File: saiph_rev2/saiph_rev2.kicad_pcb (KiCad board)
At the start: 2 copper layers, 347.7 x 126.6 mm, 211 parts, among them J1 USB_mini_micro_B, J2 Conn_01x04, M1 MISC, SW1 SW_PUSH, SW10 SW_PUSH, SW100 SW_PUSH, SW101 SW_PUSH, SW102 SW_PUSH, SW103 SW_PUSH, SW104 SW_PUSH, SW105 SW_PUSH, SW108 SKQGABE010, SW109 SW_PUSH, SW11 SW_PUSH, SW110 SW_PUSH, SW111 SW_PUSH, SW112 SKQGABE010, SW12 SW_PUSH, SW13 SW_PUSH, SW14 SW_PUSH, SW15 SW_PUSH, SW16 SW_PUSH, SW17 SW_PUSH, SW18 SW_PUSH, SW19 SW_PUSH, SW2 SW_PUSH, SW20 SW_PUSH, SW21 SW_PUSH, SW22 SW_PUSH, SW23 SW_PUSH, SW24 SW_PUSH, SW25 SW_PUSH, SW26 SW_PUSH, SW27 SW_PUSH, SW28 SW_PUSH, SW29 SW_PUSH, SW3 SW_PUSH, SW30 SW_PUSH, SW31 SW_PUSH, SW32 SW_PUSH, SW33 SW_PUSH, SW34 SW_PUSH, SW35 SW_PUSH, SW36 SW_PUSH, SW37 SW_PUSH, SW38 SW_PUSH, SW39 SW_PUSH, SW4 SW_PUSH, SW40 SW_PUSH, SW41 SW_PUSH, SW42 SW_PUSH, SW43 SW_PUSH, SW44 SW_PUSH, SW45 SW_PUSH, SW46 SW_PUSH, SW47 SW_PUSH, SW48 SW_PUSH, SW49 SW_PUSH, SW5 SW_PUSH, SW50 SW_PUSH, SW51 SW_PUSH, SW52 SW_PUSH, SW53 SW_PUSH, SW54 SW_PUSH, SW55 SW_PUSH, SW56 SW_PUSH, SW57 SW_PUSH, SW58 SW_PUSH, SW59 SW_PUSH, SW6 SW_PUSH, SW60 SW_PUSH, SW61 SW_PUSH, SW62 SW_PUSH, SW63 SW_PUSH, SW64 SW_PUSH, SW65 SW_PUSH, SW66 SW_PUSH, SW67 SW_PUSH, SW68 SW_PUSH, SW69 SW_PUSH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

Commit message: place r4 diodes
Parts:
- moved D72 7.37 mm to (245.2, 71.3), turned to 90 degrees
- moved D35 1.03 mm to (119.0, 71.3)
- moved D31 0.76 mm to (100.0, 63.7)
- moved D96 0.61 mm to (319.1, 63.7)
- moved D51 0.57 mm to (176.2, 63.7)
- moved D61 0.55 mm to (214.3, 63.7)
- moved D46 0.50 mm to (157.2, 71.3)
- moved D56 0.48 mm to (195.2, 71.3)
- moved D26 0.30 mm to (81.0, 71.3)
- moved D21 0.22 mm to (62.0, 63.7)
- moved D84 0.16 mm to (281.0, 63.7)
- moved D15 0.12 mm to (42.9, 71.3)
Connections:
- D72 pad 1: Net-(D72-K) -> /R3
- D72 pad 2: /R3 -> Net-(D72-A)
- SW72 pad 2: Net-(D72-K) -> Net-(D72-A)
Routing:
- net /R3: track 87.8 -> 93.1 mm
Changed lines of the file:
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@@
   (net 76 "Net-(D70-K)")
   (net 77 "Net-(D71-K)")
-  (net 78 "Net-(D72-K)")
+  (net 78 "Net-(D72-A)")
   (net 79 "Net-(D73-K)")
   (net 80 "Net-(D74-K)")
@@
   )
   (footprint "Diodes_ThroughHole:D_DO-35_SOD27_P7.62mm_Horizontal" (layer "F.Cu")
-    (at 42.75 71.325 90)
+    (at 42.875 71.325 90)
     (descr "D, DO-35_SOD27 series, Axial, Horizontal, pin pitch=7.62mm, , length*diameter=4*2mm^2, , http://www.diodes.com/_files/packages/DO-35.pdf")
     (tags "D DO-35_SOD27 series Axial Horizontal pin pitch 7.62mm  length 4mm diameter 2mm")
@@
   )
   (footprint "Diodes_ThroughHole:D_DO-35_SOD27_P7.62mm_Horizontal" (layer "F.Cu")
-    (at 62 63.925 -90)
+    (at 62 63.705 -90)
     (descr "D, DO-35_SOD27 series, Axial, Horizontal, pin pitch=7.62mm, , length*diameter=4*2mm^2, , http://www.diodes.com/_files/packages/DO-35.pdf")
     (tags "D DO-35_SOD27 series Axial Horizontal pin pitch 7.62mm  length 4mm diameter 2mm")
@@
   )
   (footprint "Diodes_ThroughHole:D_DO-35_SOD27_P7.62mm_Horizontal" (layer "F.Cu")
-    (at 81.14 71.575 90)
+    (at 80.975 71.325 90)
     (descr "D, DO-35_SOD27 series, Axial, Horizontal, pin pitch=7.62mm, , length*diameter=4*2mm^2, , http://www.diodes.com/_files/packages/DO-35.pdf")
     (tags "D DO-35_SOD27 series Axial Horizontal pin pitch 7.62mm  length 4mm diameter 2mm")
@@
   )
   (footprint "Diodes_ThroughHole:D_DO-35_SOD27_P7.62mm_Horizontal" (layer "F.Cu")
-    (at 99.49 64.27 -90)
+    (at 100 63.705 -90)
     (descr "D, DO-35_SOD27 series, Axial, Horizontal, pin pitch=7.62mm, , length*diameter=4*2mm^2, , http://www.diodes.com/_files/packages/DO-35.pdf")
     (tags "D DO-35_SOD27 series Axial Horizontal pin pitch 7.62mm  length 4mm diameter 2mm")
@@
   )
   (footprint "Diodes_ThroughHole:D_DO-35_SOD27_P7.62mm_Horizontal" (layer "F.Cu")
-    (at 120.05 71.255 90)
+    (at 119.025 71.325 90)
     (descr "D, DO-35_SOD27 series, Axial, Horizontal, pin pitch=7.62mm, , length*diameter=4*2mm^2, , http://www.diodes.com/_files/packages/DO-35.pdf")
     (tags "D DO-35_SOD27 series Axial Horizontal pin pitch 7.62mm  length 4mm diameter 2mm")
@@
   )
   (footprint "Diodes_ThroughHole:D_DO-35_SOD27_P7.62mm_Horizontal" (layer "F.Cu")
-    (at 138.17 63.675 -90)
+    (at 138.17 63.705 -90)
     (descr "D, DO-35_SOD27 series, Axial, Horizontal, pin pitch=7.62mm, , length*diameter=4*2mm^2, , http://www.diodes.com/_files/packages/DO-35.pdf")
     (tags "D DO-35_SOD27 series Axial Horizontal pin pitch 7.62mm  length 4mm diameter 2mm")
@@
   )
   (footprint "Diodes_ThroughHole:D_DO-35_SOD27_P7.62mm_Horizontal" (layer "F.Cu")
-    (at 157.25 70.825 90)
+    (at 157.25 71.325 90)
     (descr "D, DO-35_SOD27 series, Axial, Horizontal, pin pitch=7.62mm, , length*diameter=4*2mm^2, , http://www.diodes.com/_files/packages/DO-35.pdf")
     (tags "D DO-35_SOD27 series Axial Horizontal pin pitch 7.62mm  length 4mm diameter 2mm")
@@
   )
   (footprint "Diodes_ThroughHole:D_DO-35_SOD27_P7.62mm_Horizontal" (layer "F.Cu")
-    (at 176 63.175 -90)
+    (at 176.2 63.705 -90)
     (descr "D, DO-35_SOD27 series, Axial, Horizontal, pin pitch=7.62mm, , length*diameter=4*2mm^2, , http://www.diodes.com/_files/packages/DO-35.pdf")
     (tags "D DO-35_SOD27 series Axial Horizontal pin pitch 7.62mm  length 4mm diameter 2mm")
@@
   )
   (footprint "Diodes_ThroughHole:D_DO-35_SOD27_P7.62mm_Horizontal" (layer "F.Cu")
-    (at 195.49 71.745 90)
+    (at 195.25 71.325 90)
     (descr "D, DO-35_SOD27 series, Axial, Horizontal, pin pitch=7.62mm, , length*diameter=4*2mm^2, , http://www.diodes.com/_files/packages/DO-35.pdf")
     (tags "D DO-35_SOD27 series Axial Horizontal pin pitch 7.62mm  length 4mm diameter 2mm")
@@
   )
   (footprint "Diodes_ThroughHole:D_DO-35_SOD27_P7.62mm_Horizontal" (layer "F.Cu")
-    (at 214.76 64.045 -90)
+    (at 214.325 63.705 -90)
     (descr "D, DO-35_SOD27 series, Axial, Horizontal, pin pitch=7.62mm, , length*diameter=4*2mm^2, , http://www.diodes.com/_files/packages/DO-35.pdf")
     (tags "D DO-35_SOD27 series Axial Horizontal pin pitch 7.62mm  length 4mm diameter 2mm")
@@
   )
   (footprint "Diodes_ThroughHole:D_DO-35_SOD27_P7.62mm_Horizontal" (layer "F.Cu")
-    (at 245.18 63.955 -90)
+    (at 245.25 71.325 90)
     (descr "D, DO-35_SOD27 series, Axial, Horizontal, pin pitch=7.62mm, , length*diameter=4*2mm^2, , http://www.diodes.com/_files/packages/DO-35.pdf")
     (tags "D DO-35_SOD27 series Axial Horizontal pin pitch 7.62mm  length 4mm diameter 2mm")
@@
     (fp_line (start 7.62 0) (end 5.81 0)
       (stroke (width 0.1) (type solid)) (layer "F.Fab"))
-    (pad "1" thru_hole rect (at 0 0 270) (size 1.6 1.6) (drill 0.8) (layers "*.Cu" "*.Mask")
-      (net 78 "Net-(D72-K)") (pinfunction "K") (pintype "passive"))
-    (pad "2" thru_hole oval (at 7.62 0 270) (size 1.6 1.6) (drill 0.8) (layers "*.Cu" "*.Mask")
-      (net 8 "/R3") (pinfunction "A") (pintype "passive"))
+    (pad "1" thru_hole rect (at 0 0 90) (size 1.6 1.6) (drill 0.8) (layers "*.Cu" "*.Mask")
+      (net 8 "/R3") (pinfunction "K") (pintype "passive"))
+    (pad "2" thru_hole oval (at 7.62 0 90) (size 1.6 1.6) (drill 0.8) (layers "*.Cu" "*.Mask")
+      (net 78 "Net-(D72-A)") (pinfunction "A") (pintype "passive"))
     (model "${KISYS3DMOD}/Diodes_THT.3dshapes/D_DO-35_SOD27_P7.62mm_Horizontal.wrl"
       (offset (xyz 0 0 0))
@@
   )
   (footprint "Diodes_ThroughHole:D_DO-35_SOD27_P7.62mm_Horizontal" (layer "F.Cu")
-    (at 281 63.865 -90)
+    (at 281 63.705 -90)
     (descr "D, DO-35_SOD27 series, Axial, Horizontal, pin pitch=7.62mm, , length*diameter=4*2mm^2, , http://www.diodes.com/_files/packages/DO-35.pdf")
     (tags "D DO-35_SOD27 series Axial Horizontal pin pitch 7.62mm  length 4mm diameter 2mm")
@@
   )
   (footprint "Diodes_ThroughHole:D_DO-35_SOD27_P7.62mm_Horizontal" (layer "F.Cu")
-    (at 300.05 71.275 90)
+    (at 300.05 71.325 90)
     (descr "D, DO-35_SOD27 series, Axial, Horizontal, pin pitch=7.62mm, , length*diameter=4*2mm^2, , http://www.diodes.com/_files/packages/DO-35.pdf")
     (tags "D DO-35_SOD27 series Axial Horizontal pin pitch 7.62mm  length 4mm diameter 2mm")
@@
   )
   (footprint "Diodes_ThroughHole:D_DO-35_SOD27_P7.62mm_Horizontal" (layer "F.Cu")
-    (at 319.05 63.095 -90)
+    (at 319.05 63.705 -90)
     (descr "D, DO-35_SOD27 series, Axial, Horizontal, pin pitch=7.62mm, , length*diameter=4*2mm^2, , http://www.diodes.com/_files/packages/DO-35.pdf")
     (tags "D DO-35_SOD27 series Axial Horizontal pin pitch 7.62mm  length 4mm diameter 2mm")
@@
       (net 107 "/C6") (pinfunction "1") (pintype "passive"))
     (pad "2" thru_hole circle (at -5.75 -2.5 90) (size 2.5 2.5) (drill 1.5) (layers "*.Cu" "*.Mask" "F.SilkS")
-      (net 78 "Net-(D72-K)") (pinfunction "2") (pintype "passive"))
+      (net 78 "Net-(D72-A)") (pinfunction "2") (pintype "passive"))
     (pad "3" thru_hole circle (at 5.75 -5.999988 90) (size 2.5 2.5) (drill 1.5) (layers "*.Cu" "*.Mask" "F.SilkS"))
     (pad "3" thru_hole circle (at 5.75 5.999988 90) (size 2.5 2.5) (drill 1.5) (layers "*.Cu" "*.Mask" "F.SilkS"))
@@
   (segment (start 290.637 3.65) (end 285.699552 8.587448) (width 0.1524) (layer "F.Cu") (net 5))
   (via (at 290.637 3.65) (size 0.6) (drill 0.3) (layers "F.Cu" "B.Cu") (net 5))
-  (segment (start 251.203912 65.551088) (end 245.18 71.575) (width 0.1524) (layer "F.Cu") (net 8))
   (segment (start 290.637 5.65) (end 286.004352 10.282648) (width 0.1524) (layer "F.Cu") (net 8))
-  (segment (start 256.3902 65.551088) (end 251.203912 65.551088) (width 0.1524) (layer "F.Cu") (net 8))
   (segment (start 286.004352 35.936936) (end 256.3902 65.551088) (width 0.1524) (layer "F.Cu") (net 8))
+  (segment (start 319.05 71.325) (end 300.05 71.325) (width 0.1524) (layer "F.Cu") (net 8))
   (segment (start 286.004352 10.282648) (end 286.004352 35.936936) (width 0.1524) (layer "F.Cu") (net 8))
   (via (at 290.637 5.65) (size 0.6) (drill 0.3) (layers "F.Cu" "B.Cu") (net 8))

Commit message: route more diodes
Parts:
- removed J2: Conn_01x04, Connector_PinHeader_2.54mm:PinHeader_1x04_P2.54mm_Vertical
- moved D6 35.4 mm to (-7.12, 105.4), turned to 90 degrees
- moved D66 26.0 mm to (276.2, 90.5), turned to 90 degrees
- moved D73 19.5 mm to (183.3, 97.8), turned to -90 degrees
- moved D5 14.3 mm to (0.03, 90.5), turned to 90 degrees
- moved D11 10.7 mm to (16.7, 97.8), turned to -90 degrees
- moved D17 8.58 mm to (40.5, 105.4), turned to 90 degrees
- moved D62 7.47 mm to (231.0, 82.9), turned to -90 degrees
- moved D37 6.82 mm to (112.0, 105.4), turned to 90 degrees
- moved D68 1.88 mm to (204.8, 105.4)
- moved D27 1.45 mm to (90.5, 90.5)
- moved D32 1.15 mm to (109.5, 82.9)
- moved D42 0.86 mm to (147.6, 82.9)
- moved D36 0.82 mm to (128.5, 90.5)
- moved D80 0.75 mm to (252.4, 105.4)
- moved D52 0.67 mm to (185.8, 82.9)
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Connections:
- D62 pad 1: /R4 -> Net-(D62-K)
- D62 pad 2: Net-(D62-A) -> /R4
- SW62 pad 1: /C6 -> /C5
- SW62 pad 2: Net-(D62-A) -> Net-(D62-K)
- SW66 pad 1: /C6 -> /C5
- SW66 pad 2: Net-(D62-A) -> Net-(D62-K)
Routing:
- net /R5: track 40.5 -> 422.0 mm
- net /R4: track 100.5 -> 416.6 mm
- net /R2: track 74.1 -> 357.6 mm
- net /R3: track 93.1 -> 363.8 mm
- net /C6: track 31.0 -> 54.8 mm
- net Net-(D66-A): track 0.00 -> 17.1 mm
- net Net-(D62-K): track 0.00 -> 15.5 mm
- net Net-(D37-A): track 0.00 -> 13.4 mm
- net /C5: track 67.6 -> 77.1 mm
- net /C3: track 152.6 -> 162.1 mm
- net Net-(D68-A): track 0.00 -> 8.65 mm
- net Net-(D5-A): track 0.00 -> 7.97 mm
- net Net-(D17-A): track 0.00 -> 6.28 mm
- net Net-(D42-K): track 0.00 -> 6.03 mm
- net Net-(D36-A): track 0.00 -> 6.03 mm
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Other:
- outline, holes or cut-outs redrawn

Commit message: route more diodes
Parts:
- moved D7 7.98 mm to (9.48, 25.8), turned to -90 degrees
- moved D2 5.91 mm to (-4.75, 33.4), turned to -90 degrees
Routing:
- net /C1: track 223.3 -> 475.5 mm
- net /R1: track 36.5 -> 279.4 mm
- net /C8: track 0.00 -> 237.3 mm
- net /C2: track 203.1 -> 386.2 mm
- net /C4: track 115.5 -> 289.6 mm
- net /C6: track 54.8 -> 213.8 mm
- net /C5: track 77.1 -> 231.6 mm
- net /C0: track 312.4 -> 442.2 mm
- net /C7: track 6.74 -> 110.4 mm
- net /R5: track 422.0 -> 512.0 mm
- net /C3: track 162.1 -> 202.3 mm
- net Net-(D2-A): track 0.00 -> 22.0 mm
- net /R0: track 301.7 -> 320.7 mm
- net /R2: track 357.6 -> 374.3 mm
- net Net-(D70-K): track 0.00 -> 15.6 mm
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
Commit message: route more diodes n' stuff (ii)
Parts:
- moved D4 14.8 mm to (16.7, 71.3), turned to 90 degrees
- moved D9 14.7 mm to (23.8, 63.7), turned to -90 degrees
- moved D3 0.60 mm to (0.49, 52.3)
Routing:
- net /C3: track 202.3 -> 373.0 mm
- net /C5: track 231.6 -> 329.1 mm
- net /C0: track 442.2 -> 529.1 mm
- net /C7: track 110.4 -> 181.1 mm
- net /C6: track 213.8 -> 281.3 mm
- net /C4: track 289.6 -> 319.0 mm
- net /R3: track 367.6 -> 393.8 mm
- net Net-(D4-A): track 0.00 -> 21.8 mm
- net /R1: track 279.4 -> 298.4 mm
- net /R2: track 374.3 -> 392.9 mm
- net Net-(D3-A): track 0.00 -> 14.5 mm
- net Net-(D94-K): track 0.00 -> 6.04 mm
- net Net-(D88-A): track 0.00 -> 6.02 mm
- net Net-(D9-K): track 0.00 -> 5.86 mm

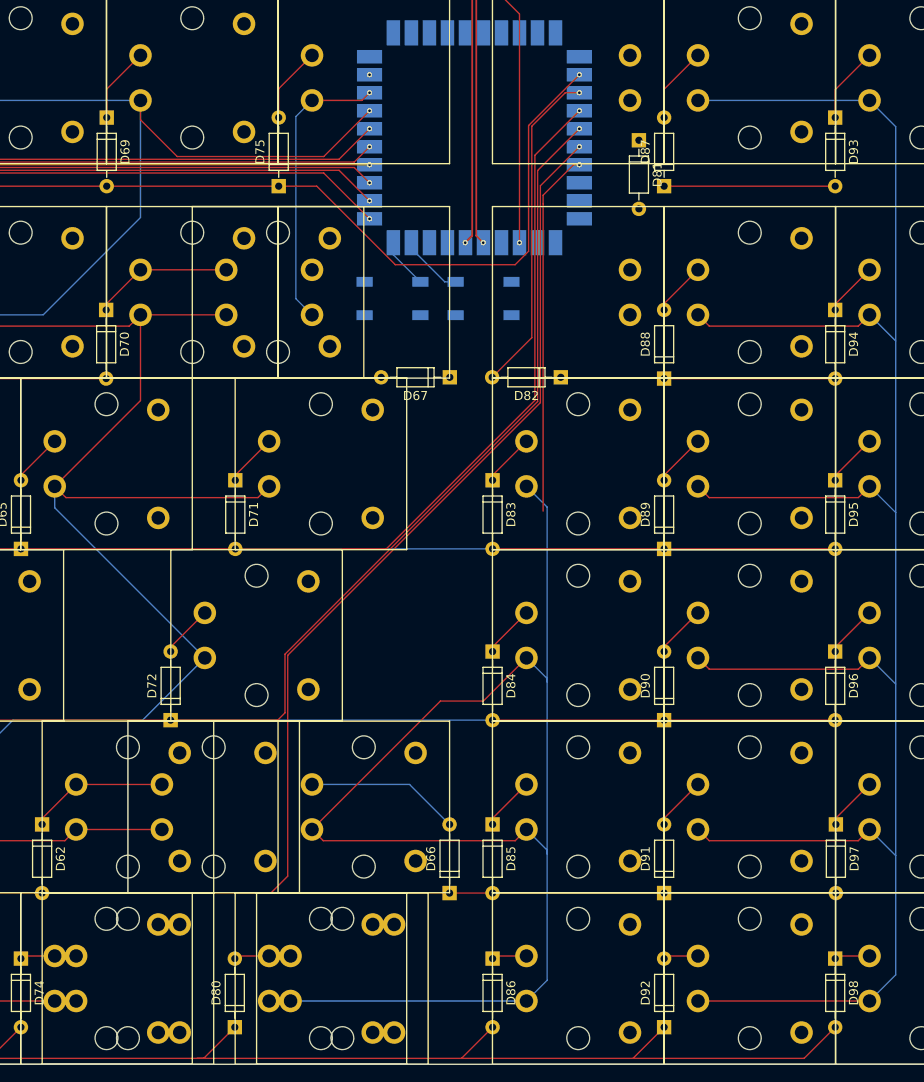
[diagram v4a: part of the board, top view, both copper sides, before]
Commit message: routing pretty much done.
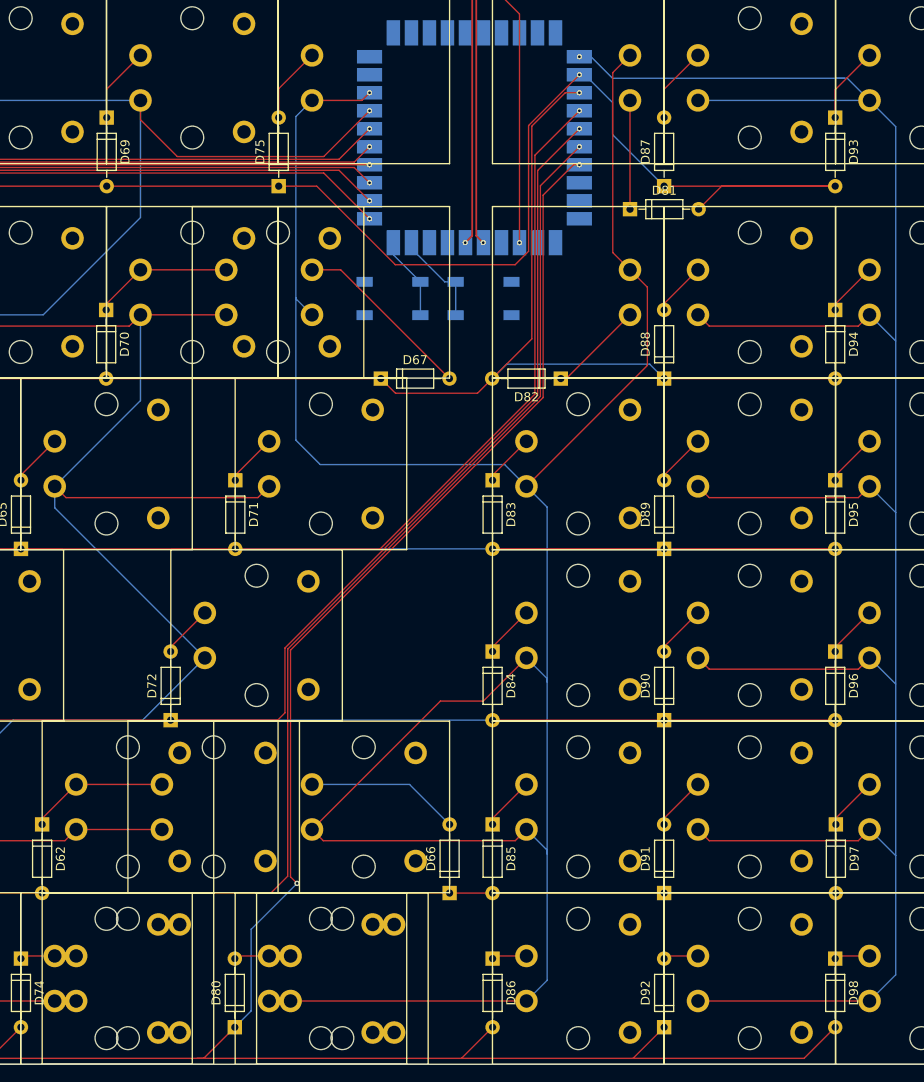
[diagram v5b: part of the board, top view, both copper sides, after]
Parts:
- moved D81 7.72 mm to (296.3, 14.6), turned to 0 degrees
- moved D67 7.66 mm to (268.6, 33.4), turned to 0 degrees
- moved D82 0.14 mm to (288.6, 33.4)
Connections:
- U1 pad 21: unconnected-(U1-GPIO20-Pad21) -> /C8
- U1 pad 9: /C8 -> unconnected-(U1-GPIO8-Pad9)
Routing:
- net /C7: track 181.1 -> 280.5 mm
- net /R5: track 512.0 -> 584.1 mm, vias 1 -> 2
- net /R1: track 298.4 -> 363.1 mm
- net /C8: track 237.3 -> 272.4 mm
- net /R0: track 320.7 -> 353.5 mm
- net Net-(D67-A): track 0.00 -> 20.3 mm
- net Net-(D81-K): track 0.00 -> 12.1 mm
- net Net-(D82-K): track 0.00 -> 10.6 mm
- net /NRST: track 7.10 -> 10.8 mm
- net /BOOTSEL: track 5.59 -> 9.29 mm
